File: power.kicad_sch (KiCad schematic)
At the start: 43 parts, among them U1 MAX20008AFOA/VY+, U2 AP63205WU, U3 AP63203WU, U8 INA190A4IDCKR

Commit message: add logo and use 0603 LEDs
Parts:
- D10, D8, D9: footprint ProjectLibrary:LED_0402_1005Metric -> LED_SMD:LED_0603_1608Metric
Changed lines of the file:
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@@
 			)
 		)
-		(property "Footprint" "ProjectLibrary:LED_0402_1005Metric"
+		(property "Footprint" "LED_SMD:LED_0603_1608Metric"
 			(at 105.41 184.15 0)
 			(effects
@@
 			)
 		)
-		(property "Footprint" "ProjectLibrary:LED_0402_1005Metric"
+		(property "Footprint" "LED_SMD:LED_0603_1608Metric"
 			(at 87.63 184.15 0)
 			(effects
@@
 			)
 		)
-		(property "Footprint" "ProjectLibrary:LED_0402_1005Metric"
+		(property "Footprint" "LED_SMD:LED_0603_1608Metric"
 			(at 123.19 184.15 0)
 			(effects

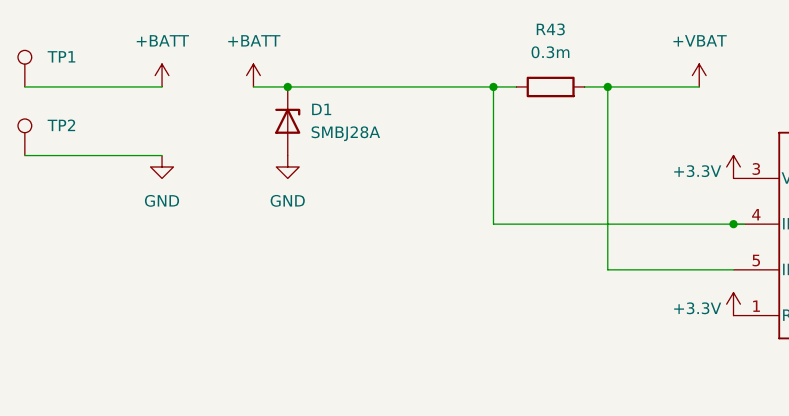
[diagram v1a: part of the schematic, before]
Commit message: change LED footprint to 0603 and change D1 to more powerful diode with same footprint
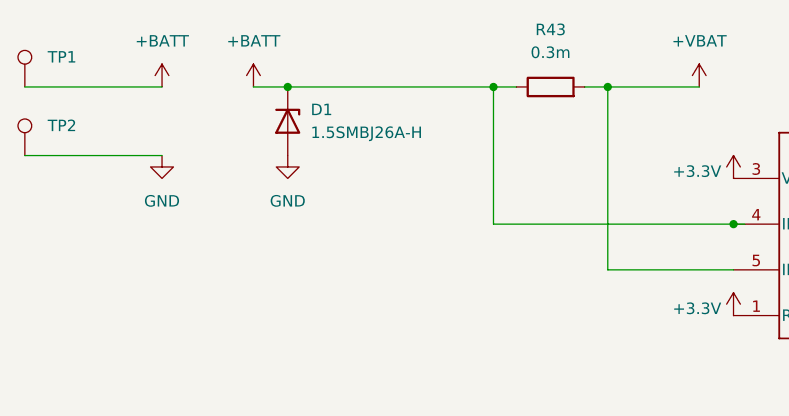
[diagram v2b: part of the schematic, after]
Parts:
- D1: value SMBJ28A -> 1.5SMBJ26A-H; Amps (none) -> 35; Part Number (none) -> 1.5SMBJ26A-H; Voltage (none) -> 42
- D10, D8, D9: Manufacturer Vishay -> Lite-On; Part Number VLMG1500-GS08 -> LTST-C191GKT; Voltage (none) -> 2
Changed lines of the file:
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@@
 			)
 		)
-		(property "Manufacturer" "Vishay"
+		(property "Manufacturer" "Lite-On"
 			(at 105.41 184.15 0)
 			(effects
@@
 			)
 		)
-		(property "Part Number" "VLMG1500-GS08"
+		(property "Part Number" "LTST-C191GKT"
+			(at 105.41 184.15 0)
+			(effects
+				(font
+					(size 1.27 1.27)
+				)
+				(hide yes)
+			)
+		)
+		(property "Voltage" "2"
 			(at 105.41 184.15 0)
 			(effects
@@
 			)
 		)
-		(property "Value" "SMBJ28A"
+		(property "Value" "1.5SMBJ26A-H "
 			(at 54.61 30.4799 90)
 			(effects
@@
 			)
 		)
+		(property "Part Number" "1.5SMBJ26A-H "
+			(at 52.07 29.21 0)
+			(effects
+				(font
+					(size 1.27 1.27)
+				)
+				(hide yes)
+			)
+		)
+		(property "Voltage" "42"
+			(at 52.07 29.21 0)
+			(effects
+				(font
+					(size 1.27 1.27)
+				)
+				(hide yes)
+			)
+		)
+		(property "Amps" "35"
+			(at 52.07 29.21 0)
+			(effects
+				(font
+					(size 1.27 1.27)
+				)
+				(hide yes)
+			)
+		)
 		(pin "2"
 		)
@@
 			)
 		)
-		(property "Manufacturer" "Vishay"
+		(property "Manufacturer" "Lite-On"
+			(at 87.63 184.15 0)
+			(effects
+				(font
+					(size 1.27 1.27)
+				)
+				(hide yes)
+			)
+		)
+		(property "Part Number" "LTST-C191GKT"
 			(at 87.63 184.15 0)
 			(effects
@@
 			)
 		)
-		(property "Part Number" "VLMG1500-GS08"
+		(property "Voltage" "2"
 			(at 87.63 184.15 0)
 			(effects
@@
 			)
 		)
-		(property "Manufacturer" "Vishay"
+		(property "Manufacturer" "Lite-On"
+			(at 123.19 184.15 0)
+			(effects
+				(font
+					(size 1.27 1.27)
+				)
+				(hide yes)
+			)
+		)
+		(property "Part Number" "LTST-C191GKT"
 			(at 123.19 184.15 0)
 			(effects
@@
 			)
 		)
-		(property "Part Number" "VLMG1500-GS08"
+		(property "Voltage" "2"
 			(at 123.19 184.15 0)
 			(effects

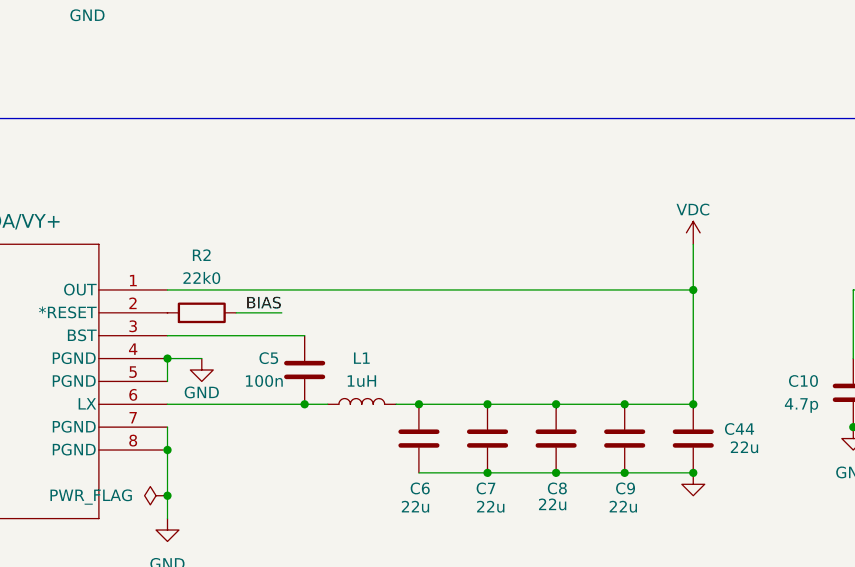
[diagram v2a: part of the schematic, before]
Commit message: remove blind vias
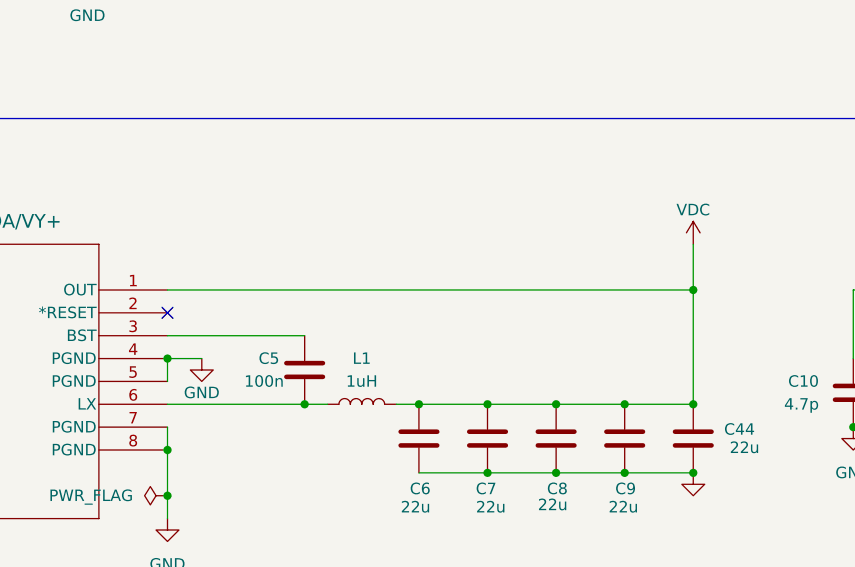
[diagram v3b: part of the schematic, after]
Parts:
- removed R2: 22k0, Resistor_SMD:R_0402_1005Metric, symbol Device:R
- C23, C24: footprint Capacitor_SMD:C_0603_1608Metric -> Capacitor_SMD:C_0402_1005Metric; Manufacturer YAGEO -> Murata; Part Number CC0603KRX5R9BB105 -> GRM155R61H105KE05D
- R1, R3, R38, R39, R40: footprint Resistor_SMD:R_0402_1005Metric -> ProjectLibrary:R_0201_0603Metric
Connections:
- no-connect marks 0 -> 1
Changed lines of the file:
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@@
 		(color 0 0 0 0)
 	)
+	(no_connect
+		(at 146.05 88.9)
+	)
 	(wire
 		(pts
@@
 	(wire
 		(pts
-			(xy 158.75 88.9) (xy 153.67 88.9)
-		)
-		(stroke
-			(width 0)
-			(type default)
-		)
-	)
-	(wire
-		(pts
 			(xy 222.25 93.98) (xy 222.25 86.36)
 		)
@@
 	(wire
 		(pts
-			(xy 204.47 86.36) (xy 146.05 86.36)
+			(xy 173.99 99.06) (xy 181.61 99.06)
 		)
 		(stroke
@@
 	(wire
 		(pts
-			(xy 173.99 99.06) (xy 181.61 99.06)
+			(xy 146.05 86.36) (xy 204.47 86.36)
 		)
 		(stroke
@@
 		)
 	)
-	(label "BIAS"
-		(at 158.75 88.9 180)
-		(fields_autoplaced yes)
-		(effects
-			(font
-				(size 1.27 1.27)
-			)
-			(justify right bottom)
-		)
-	)
 	(global_label "CURR"
 		(shape output)
@@
 			)
 		)
-		(property "Footprint" "Resistor_SMD:R_0402_1005Metric"
+		(property "Footprint" "ProjectLibrary:R_0201_0603Metric"
 			(at 85.852 176.53 90)
 			(effects
@@
 			)
 		)
-		(property "Footprint" "Resistor_SMD:R_0402_1005Metric"
+		(property "Footprint" "ProjectLibrary:R_0201_0603Metric"
 			(at 103.632 176.53 90)
 			(effects
@@
 			)
 		)
-		(property "Footprint" "Capacitor_SMD:C_0603_1608Metric"
+		(property "Footprint" "Capacitor_SMD:C_0402_1005Metric"
 			(at 50.4952 186.69 0)
 			(effects
@@
 			)
 		)
-		(property "Part Number" "CC0603KRX5R9BB105"
+		(property "Part Number" "GRM155R61H105KE05D"
 			(at 49.53 182.88 0)
 			(effects
@@
 			)
 		)
-		(property "Manufacturer" "YAGEO"
+		(property "Manufacturer" "Murata"
 			(at 49.53 182.88 0)
 			(effects
@@
 			)
 		)
-		(property "Footprint" "Capacitor_SMD:C_0603_1608Metric"
+		(property "Footprint" "Capacitor_SMD:C_0402_1005Metric"
 			(at 63.1952 186.69 0)
 			(effects
@@
 			)
 		)
-		(property "Part Number" "CC0603KRX5R9BB105"
+		(property "Part Number" "GRM155R61H105KE05D"
 			(at 62.23 182.88 0)
 			(effects
@@
 			)
 		)
-		(property "Manufacturer" "YAGEO"
+		(property "Manufacturer" "Murata"
 			(at 62.23 182.88 0)
 			(effects
@@
 			)
 		)
-		(property "Footprint" "Resistor_SMD:R_0402_1005Metric"
+		(property "Footprint" "ProjectLibrary:R_0201_0603Metric"
 			(at 96.52 88.138 90)
 			(effects
@@
 	)
 	(symbol
-		(lib_id "Device:R")
-		(at 149.86 88.9 270)
-		(mirror x)
-		(unit 1)
-		(exclude_from_sim no)
-		(in_bom yes)
-		(on_board yes)
-		(dnp no)
-		(fields_autoplaced yes)
-		(property "Reference" "R2"
-			(at 149.86 82.55 90)
-			(effects
-				(font
-					(size 1.27 1.27)
-				)
-			)
-		)
-		(property "Value" "22k0"
-			(at 149.86 85.09 90)
-			(effects
-				(font
-					(size 1.27 1.27)
-				)
-			)
-		)
-		(property "Footprint" "Resistor_SMD:R_0402_1005Metric"
-			(at 149.86 90.678 90)
-			(effects
-				(font
-					(size 1.27 1.27)
-				)
-				(hide yes)
-			)
-		)
-		(property "Datasheet" "~"
-			(at 149.86 88.9 0)
-			(effects
-				(font
-					(size 1.27 1.27)
-				)
-				(hide yes)
-			)
-		)
-		(property "Description" "Resistor"
-			(at 149.86 88.9 0)
-			(effects
-				(font
-					(size 1.27 1.27)
-				)
-				(hide yes)
-			)
-		)
-		(property "Manufacturer" "YAGEO"
-			(at 149.86 88.9 0)
-			(effects
-				(font
-					(size 1.27 1.27)
-				)
-				(hide yes)
-			)
-		)
-		(property "Part Number" "RC0402FR-0722KL"
-			(at 149.86 88.9 0)
-			(effects
-				(font
-					(size 1.27 1.27)
-				)
-				(hide yes)
-			)
-		)
-		(pin "1"
-		)
-		(pin "2"
-		)
-		(instances
-			(project "ESC BB21"
-				(path "/d268946a-c85a-4346-a268-ba5c3792dae2/fc3226d6-c5d3-4262-b696-e1da1f3bb6f0"
-					(reference "R2")
-					(unit 1)
-				)
-			)
-		)
-	)
-	(symbol
 		(lib_id "power:+3.3V")
 		(at 87.63 172.72 0)
@@
 			)
 		)
-		(property "Footprint" "Resistor_SMD:R_0402_1005Metric"
+		(property "Footprint" "ProjectLibrary:R_0201_0603Metric"
 			(at 121.412 176.53 90)
 			(effects
@@
 			)
 		)
-		(property "Footprint" "Resistor_SMD:R_0402_1005Metric"
+		(property "Footprint" "ProjectLibrary:R_0201_0603Metric"
 			(at 232.918 90.17 90)
 			(effects

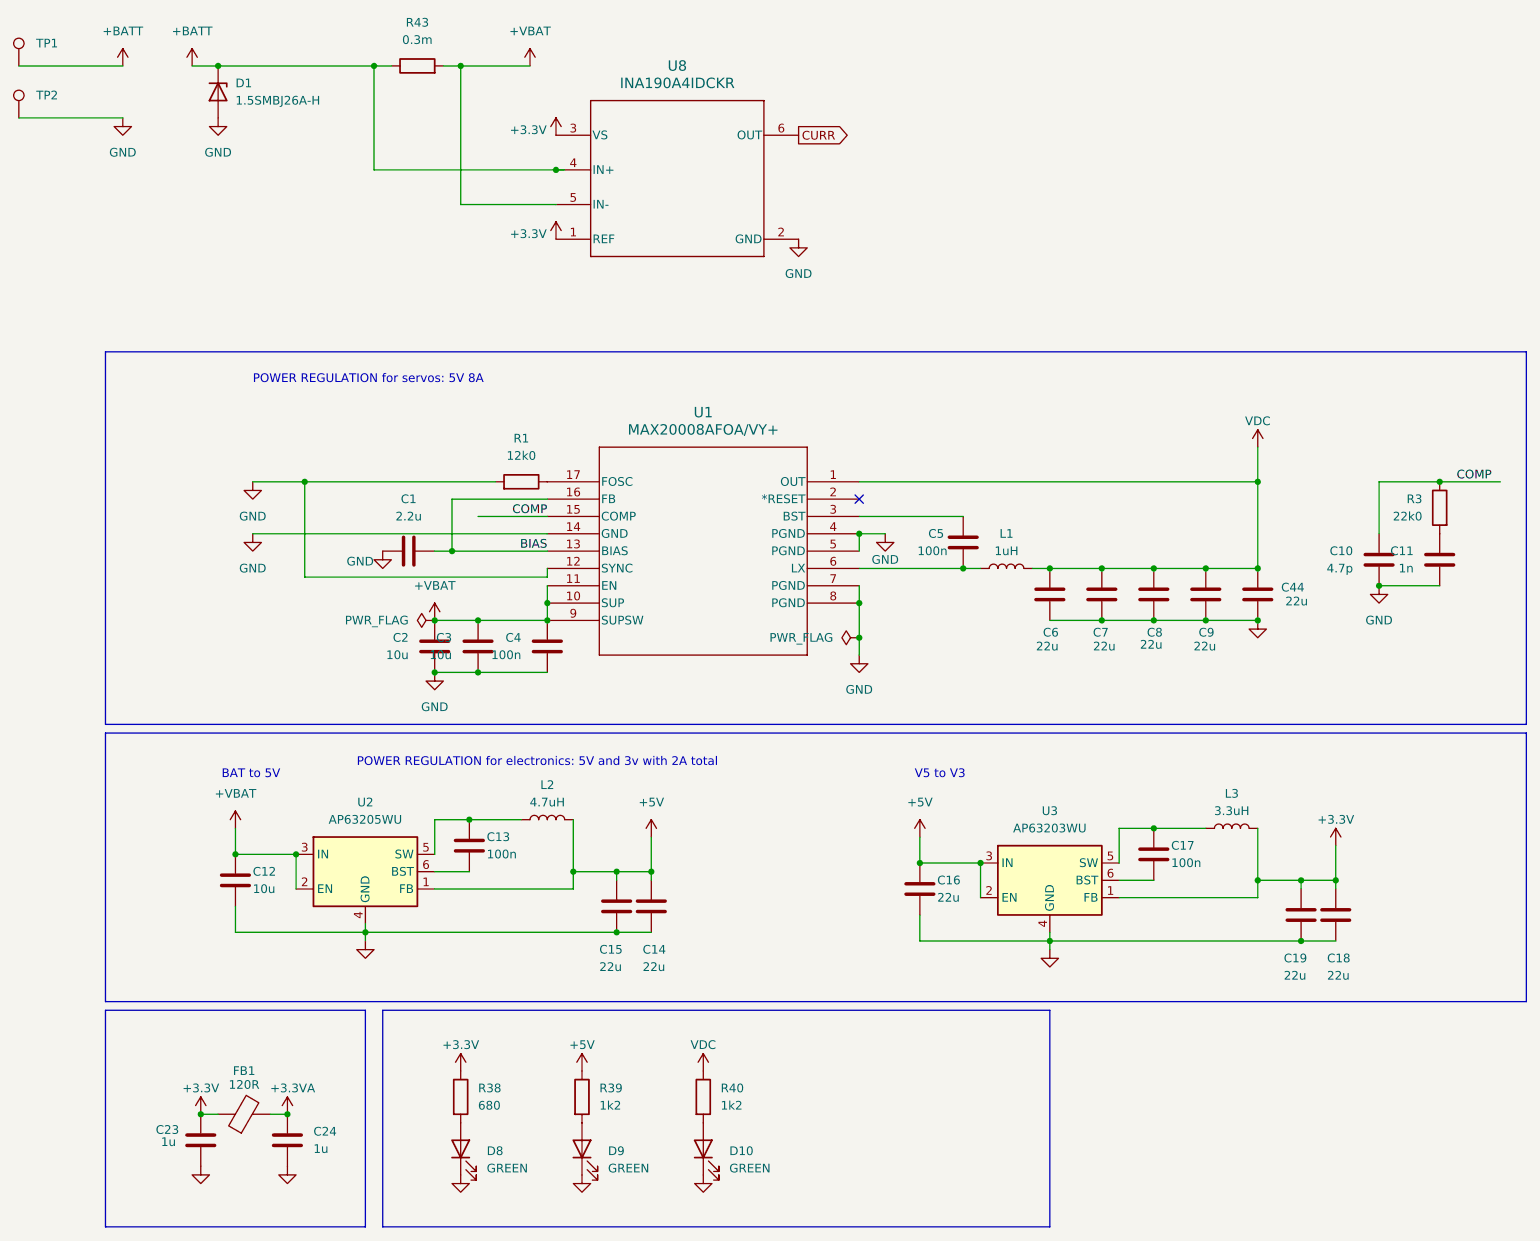
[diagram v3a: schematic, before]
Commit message: cleanup layout, silkmasks, and add connections between planes for power and gnd
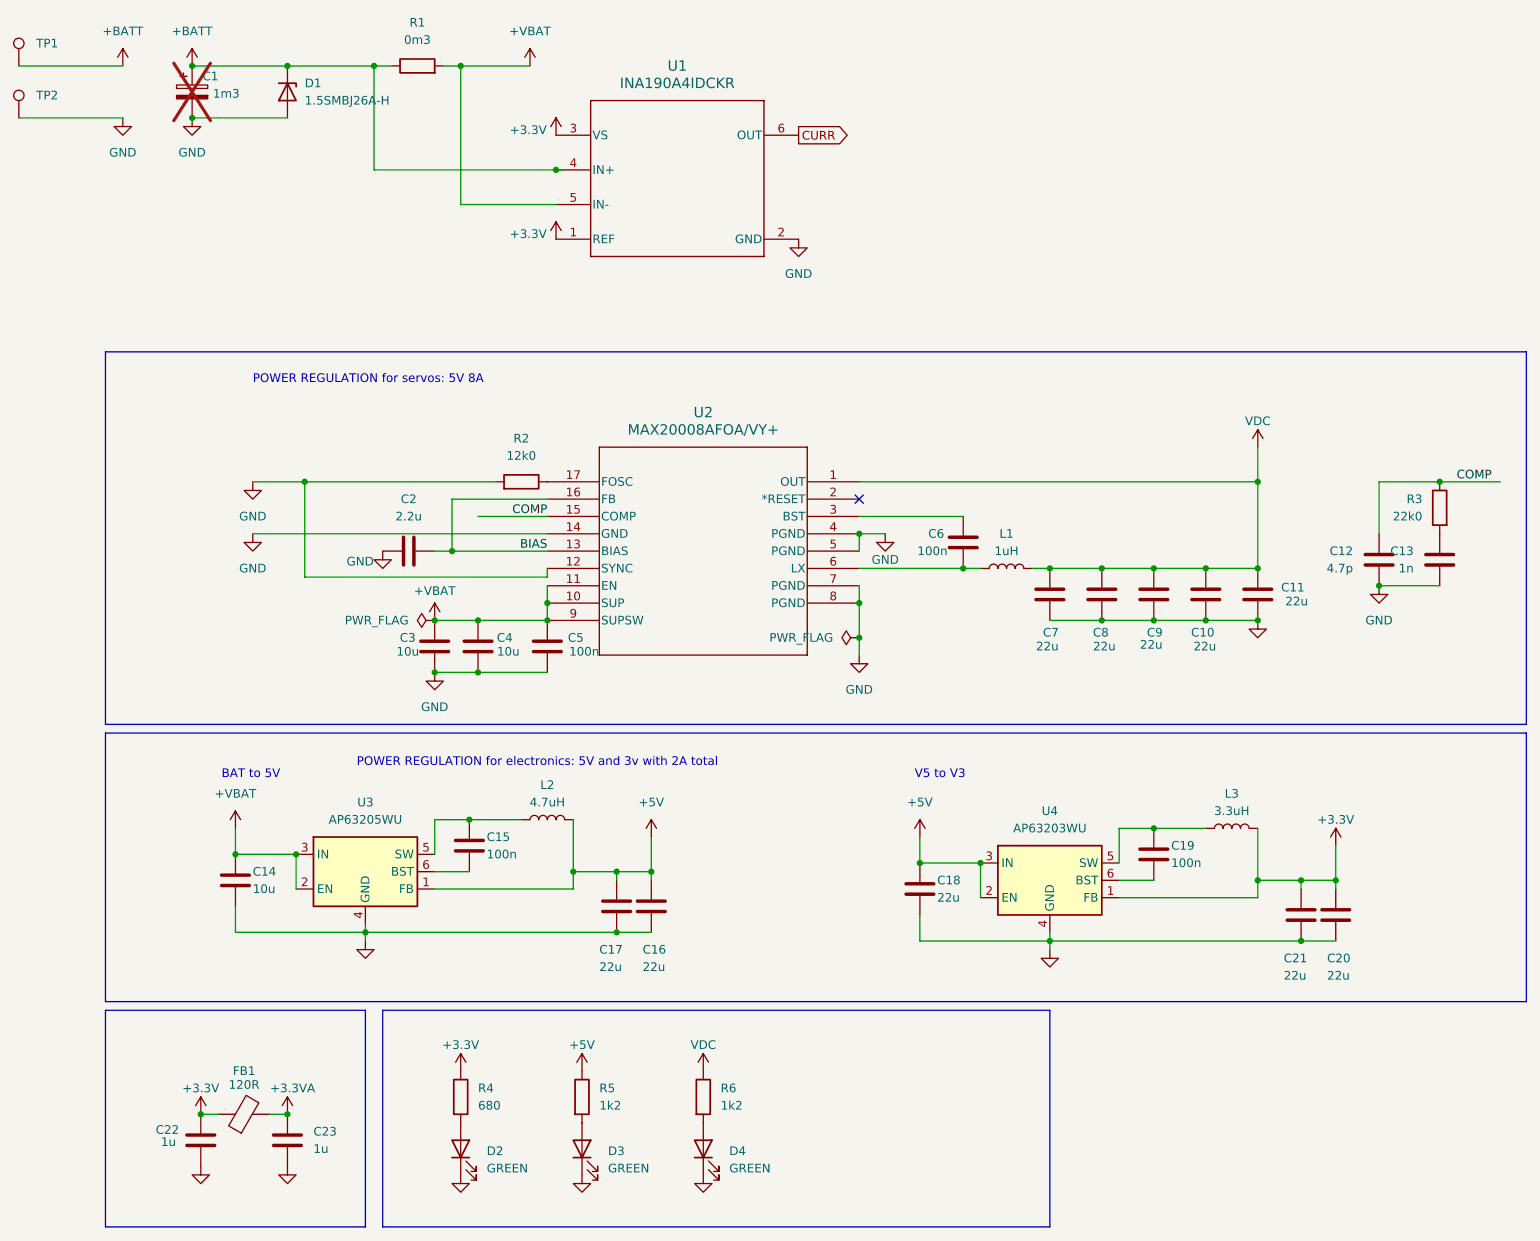
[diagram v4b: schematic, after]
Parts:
- added C1: 1m3, symbol Device:C_Polarized
- C10: renamed from C9; Manufacturer Samsung -> Murata; Part Number CL21A226MAYNNNE -> GRM21BR61E226ME44K; Tolerance (none) -> 20%
- C11: renamed from C44; Manufacturer Samsung -> Murata; Part Number CL21A226MAYNNNE -> GRM21BR61E226ME44K; Tolerance (none) -> 20%
- C12: renamed from C10; Tolerance (none) -> 0.25p
- C13: renamed from C11; Tolerance (none) -> 10%
- C14: renamed from C12; Tolerance (none) -> 10%
- C15: renamed from C13; Tolerance (none) -> 10%
- C16: renamed from C14; Manufacturer Samsung -> Murata; Part Number CL21A226MAYNNNE -> GRM21BR61E226ME44K; Tolerance (none) -> 20%
- C17: renamed from C15; Manufacturer Samsung -> Murata; Part Number CL21A226MAYNNNE -> GRM21BR61E226ME44K; Tolerance (none) -> 20%
- C18: renamed from C16; Manufacturer Samsung -> Murata; Part Number CL21A226MAYNNNE -> GRM21BR61E226ME44K; Tolerance (none) -> 20%
- C19: renamed from C17; Tolerance (none) -> 10%
- C2: renamed from C1; Tolerance (none) -> 10%
- C20: renamed from C18; Manufacturer Samsung -> Murata; Part Number CL21A226MAYNNNE -> GRM21BR61E226ME44K; Tolerance (none) -> 20%
- C21: renamed from C19; Manufacturer Samsung -> Murata; Part Number CL21A226MAYNNNE -> GRM21BR61E226ME44K; Tolerance (none) -> 20%
- C3: renamed from C2; Tolerance (none) -> 10%
- C4: renamed from C3; Tolerance (none) -> 10%
- C5: renamed from C4; Tolerance (none) -> 10%
- C6: renamed from C5; Tolerance (none) -> 10%
- C7: renamed from C6; Manufacturer Samsung -> Murata; Part Number CL21A226MAYNNNE -> GRM21BR61E226ME44K; Tolerance (none) -> 20%
- C8: renamed from C7; Manufacturer Samsung -> Murata; Part Number CL21A226MAYNNNE -> GRM21BR61E226ME44K; Tolerance (none) -> 20%
- C9: renamed from C8; Manufacturer Samsung -> Murata; Part Number CL21A226MAYNNNE -> GRM21BR61E226ME44K; Tolerance (none) -> 20%
- R1: renamed from R43; value 0.3m -> 0m3; Tolerance (none) -> 1%
- R2: renamed from R1; Tolerance (none) -> 1%
- R3: Tolerance (none) -> 1%
- R4: renamed from R38; Tolerance (none) -> 1%
- R5: renamed from R39; Tolerance (none) -> 1%
- R6: renamed from R40; Tolerance (none) -> 1%
- U2: renamed from U1; Amps (none) -> 8; Voltage (none) -> 5
- U3: renamed from U2; Amps (none) -> 2
- U4: renamed from U3; Amps (none) -> 2
- renumbered C23 to C22, C24 to C23, D8 to D2, D9 to D3, D10 to D4, U8 to U1
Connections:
- net +BATT: now also C1.1
- net GND: now also C1.2
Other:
- moved on the sheet: D1
